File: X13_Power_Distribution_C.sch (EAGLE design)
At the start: 34 parts, among them Q1 IRF1018EPBF, Q2 310mA/60V/1.6Ω, Q3 IRF1018EPBF, Q4 IRF1018EPBF

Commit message: Version C! Uses connector C!
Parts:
- removed BRICK1, BRICK2: DIST2BRICK_B, Brick_Dist_Connector:DIST2BRICK_B
- added BRICK_A, BRICK_B: DIST2BRICK_C, Brick_Dist_Connector:DIST2BRICK_C
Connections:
- net +12V_A: now also BRICK_A.VOUT+; no longer BRICK1.VOUT+
- net +12V_B: now also BRICK_B.VOUT+; no longer BRICK2.VOUT+
- net +48V: now also BRICK_A.VIN+, BRICK_B.VIN+; no longer BRICK1.VIN+, BRICK2.VIN+
- net 12V_GND: now also BRICK_A.VOUT-, BRICK_B.VOUT-; no longer BRICK1.VOUT-, BRICK2.VOUT-
- net 48V_GND: now also BRICK_A.VIN-, BRICK_B.VIN-; no longer BRICK1.VIN-, BRICK2.VIN-
- net ALERT_1: now also BRICK_A.ALERT; no longer BRICK1.ALERT
- net ALERT_2: now also BRICK_B.ALERT; no longer BRICK2.ALERT
- net C2_1: now also BRICK_A.C2; no longer BRICK1.C2
- net C2_2: now also BRICK_B.C2; no longer BRICK2.C2
- net CLK: now also BRICK_A.CLK, BRICK_B.CLK; no longer BRICK1.CLK, BRICK2.CLK
- net DATA: now also BRICK_A.DATA, BRICK_B.DATA; no longer BRICK1.DATA, BRICK2.DATA
- net ON/OFF: now also BRICK_A.ON/OFF, BRICK_B.ON/OFF; no longer BRICK1.ON/OFF, BRICK2.ON/OFF
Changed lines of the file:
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@@
 <part name="H4" library="Mounting Holes" deviceset="6-32-HOLE" device="" package3d_urn="urn:adsk.eagle:package:24384748/2"/>
 <part name="CONVERSION" library="Dist_Convert_Connector" deviceset="DIST2CON" device=""/>
-<part name="BRICK2" library="Brick_Dist_Connector" deviceset="DIST2BRICK_B" device=""/>
-<part name="BRICK1" library="Brick_Dist_Connector" deviceset="DIST2BRICK_B" device=""/>
+<part name="BRICK_A" library="Brick_Dist_Connector" deviceset="DIST2BRICK_C" device=""/>
+<part name="BRICK_B" library="Brick_Dist_Connector" deviceset="DIST2BRICK_C" device=""/>
 </parts>
 <sheets>
@@
 <attribute name="NAME" x="40.64" y="27.432" size="1.27" layer="95"/>
 </instance>
-<instance part="BRICK2" gate="G$1" x="38.1" y="63.5" smashed="yes">
+<instance part="BRICK_A" gate="G$1" x="38.1" y="101.6" smashed="yes">
+<attribute name="NAME" x="38.608" y="110.236" size="1.778" layer="95"/>
+</instance>
+<instance part="BRICK_B" gate="G$1" x="38.1" y="63.5" smashed="yes">
 <attribute name="NAME" x="38.608" y="72.136" size="1.778" layer="95"/>
-</instance>
-<instance part="BRICK1" gate="G$1" x="38.1" y="101.6" smashed="yes">
-<attribute name="NAME" x="38.608" y="110.236" size="1.778" layer="95"/>
 </instance>
 </instances>
@@
 <wire x1="68.58" y1="106.68" x2="72.39" y2="106.68" width="0.1524" layer="91"/>
 <label x="72.39" y="106.68" size="1.778" layer="95" xref="yes"/>
-<pinref part="BRICK1" gate="G$1" pin="VOUT+"/>
+<pinref part="BRICK_A" gate="G$1" pin="VOUT+"/>
 </segment>
 </net>
@@
 <wire x1="68.58" y1="68.58" x2="72.39" y2="68.58" width="0.1524" layer="91"/>
 <label x="72.39" y="68.58" size="1.778" layer="95" xref="yes"/>
-<pinref part="BRICK2" gate="G$1" pin="VOUT+"/>
+<pinref part="BRICK_B" gate="G$1" pin="VOUT+"/>
 </segment>
 </net>
@@
 <wire x1="33.02" y1="91.44" x2="29.21" y2="91.44" width="0.1524" layer="91"/>
 <label x="29.21" y="91.44" size="1.778" layer="95" rot="R180" xref="yes"/>
-<pinref part="BRICK1" gate="G$1" pin="ON/OFF"/>
+<pinref part="BRICK_A" gate="G$1" pin="ON/OFF"/>
 </segment>
 <segment>
 <wire x1="33.02" y1="53.34" x2="29.21" y2="53.34" width="0.1524" layer="91"/>
 <label x="29.21" y="53.34" size="1.778" layer="95" rot="R180" xref="yes"/>
-<pinref part="BRICK2" gate="G$1" pin="ON/OFF"/>
+<pinref part="BRICK_B" gate="G$1" pin="ON/OFF"/>
 </segment>
 </net>
@@
 <wire x1="33.02" y1="106.68" x2="29.21" y2="106.68" width="0.1524" layer="91"/>
 <label x="29.21" y="106.68" size="1.778" layer="95" rot="R180" xref="yes"/>
-<pinref part="BRICK1" gate="G$1" pin="VIN+"/>
+<pinref part="BRICK_A" gate="G$1" pin="VIN+"/>
 </segment>
 <segment>
 <wire x1="33.02" y1="68.58" x2="29.21" y2="68.58" width="0.1524" layer="91"/>
 <label x="29.21" y="68.58" size="1.778" layer="95" rot="R180" xref="yes"/>
-<pinref part="BRICK2" gate="G$1" pin="VIN+"/>
+<pinref part="BRICK_B" gate="G$1" pin="VIN+"/>
 </segment>
 <segment>
@@
 <wire x1="33.02" y1="101.6" x2="29.21" y2="101.6" width="0.1524" layer="91"/>
 <label x="29.21" y="101.6" size="1.778" layer="95" rot="R180" xref="yes"/>
-<pinref part="BRICK1" gate="G$1" pin="VIN-"/>
+<pinref part="BRICK_A" gate="G$1" pin="VIN-"/>
 </segment>
 <segment>
 <wire x1="33.02" y1="63.5" x2="29.21" y2="63.5" width="0.1524" layer="91"/>
 <label x="29.21" y="63.5" size="1.778" layer="95" rot="R180" xref="yes"/>
-<pinref part="BRICK2" gate="G$1" pin="VIN-"/>
+<pinref part="BRICK_B" gate="G$1" pin="VIN-"/>
 </segment>
 <segment>
@@
 <wire x1="68.58" y1="86.36" x2="72.39" y2="86.36" width="0.1524" layer="91"/>
 <label x="72.39" y="86.36" size="1.778" layer="95" xref="yes"/>
-<pinref part="BRICK1" gate="G$1" pin="CLK"/>
+<pinref part="BRICK_A" gate="G$1" pin="CLK"/>
 </segment>
 <segment>
 <wire x1="68.58" y1="48.26" x2="72.39" y2="48.26" width="0.1524" layer="91"/>
 <label x="72.39" y="48.26" size="1.778" layer="95" xref="yes"/>
-<pinref part="BRICK2" gate="G$1" pin="CLK"/>
+<pinref part="BRICK_B" gate="G$1" pin="CLK"/>
 </segment>
 </net>
@@
 <wire x1="68.58" y1="96.52" x2="72.39" y2="96.52" width="0.1524" layer="91"/>
 <label x="72.39" y="96.52" size="1.778" layer="95" xref="yes"/>
-<pinref part="BRICK1" gate="G$1" pin="DATA"/>
+<pinref part="BRICK_A" gate="G$1" pin="DATA"/>
 </segment>
 <segment>
 <wire x1="68.58" y1="58.42" x2="72.39" y2="58.42" width="0.1524" layer="91"/>
 <label x="72.39" y="58.42" size="1.778" layer="95" xref="yes"/>
-<pinref part="BRICK2" gate="G$1" pin="DATA"/>
+<pinref part="BRICK_B" gate="G$1" pin="DATA"/>
 </segment>
 </net>
@@
 <wire x1="68.58" y1="101.6" x2="72.39" y2="101.6" width="0.1524" layer="91"/>
 <label x="72.39" y="101.6" size="1.778" layer="95" xref="yes"/>
-<pinref part="BRICK1" gate="G$1" pin="VOUT-"/>
+<pinref part="BRICK_A" gate="G$1" pin="VOUT-"/>
 </segment>
 <segment>
 <wire x1="68.58" y1="63.5" x2="72.39" y2="63.5" width="0.1524" layer="91"/>
 <label x="72.39" y="63.5" size="1.778" layer="95" xref="yes"/>
-<pinref part="BRICK2" gate="G$1" pin="VOUT-"/>
+<pinref part="BRICK_B" gate="G$1" pin="VOUT-"/>
 </segment>
 <segment>
@@
 <wire x1="68.58" y1="43.18" x2="72.39" y2="43.18" width="0.1524" layer="91"/>
 <label x="72.39" y="43.18" size="1.778" layer="95" xref="yes"/>
-<pinref part="BRICK2" gate="G$1" pin="C2"/>
+<pinref part="BRICK_B" gate="G$1" pin="C2"/>
 </segment>
 </net>
@@
 <wire x1="68.58" y1="81.28" x2="72.39" y2="81.28" width="0.1524" layer="91"/>
 <label x="72.39" y="81.28" size="1.778" layer="95" xref="yes"/>
-<pinref part="BRICK1" gate="G$1" pin="C2"/>
+<pinref part="BRICK_A" gate="G$1" pin="C2"/>
 </segment>
 </net>
@@
 <wire x1="68.58" y1="53.34" x2="72.39" y2="53.34" width="0.1524" layer="91"/>
 <label x="72.39" y="53.34" size="1.778" layer="95" xref="yes"/>
-<pinref part="BRICK2" gate="G$1" pin="ALERT"/>
+<pinref part="BRICK_B" gate="G$1" pin="ALERT"/>
 </segment>
 </net>
@@
 <wire x1="68.58" y1="91.44" x2="72.39" y2="91.44" width="0.1524" layer="91"/>
 <label x="72.39" y="91.44" size="1.778" layer="95" xref="yes"/>
-<pinref part="BRICK1" gate="G$1" pin="ALERT"/>
-</segment>
-</net>
+<pinref part="BRICK_A" gate="G$1" pin="ALERT"/>
+</segment>
+</net>

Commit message: Moved ON/OFF, moved a diode
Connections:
- net 48V_GND: now also D6.A
- net GND_RAW: no longer D6.A
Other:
- moved on the sheet: D6, Q1, R3
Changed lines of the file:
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@@
 <attribute name="VALUE" x="228.092" y="32.385" size="1.778" layer="96" font="vector" rot="R180" align="top-left"/>
 </instance>
-<instance part="Q1" gate="G$1" x="93.98" y="142.24" smashed="yes" rot="MR270">
-<attribute name="NAME" x="95.25" y="146.05" size="1.778" layer="95" font="vector" rot="MR0"/>
-<attribute name="VALUE" x="100.33" y="137.16" size="1.778" layer="96" font="vector" rot="MR0"/>
-</instance>
-<instance part="R3" gate="G$1" x="86.36" y="158.75" smashed="yes" rot="MR90">
-<attribute name="NAME" x="87.884" y="158.75" size="1.778" layer="95" font="vector" rot="MR90" align="bottom-center"/>
-<attribute name="VALUE" x="84.836" y="158.75" size="1.778" layer="96" font="vector" rot="MR90" align="top-center"/>
-</instance>
-<instance part="D6" gate="G$1" x="77.47" y="146.05" smashed="yes" rot="MR90">
-<attribute name="NAME" x="79.502" y="143.51" size="1.778" layer="95" font="vector" rot="MR90"/>
-<attribute name="VALUE" x="75.438" y="143.51" size="1.778" layer="96" font="vector" rot="MR90" align="top-left"/>
+<instance part="Q1" gate="G$1" x="81.28" y="142.24" smashed="yes" rot="MR270">
+<attribute name="NAME" x="82.55" y="146.05" size="1.778" layer="95" font="vector" rot="MR0"/>
+<attribute name="VALUE" x="87.63" y="137.16" size="1.778" layer="96" font="vector" rot="MR0"/>
+</instance>
+<instance part="R3" gate="G$1" x="87.63" y="158.75" smashed="yes" rot="MR90">
+<attribute name="NAME" x="89.154" y="158.75" size="1.778" layer="95" font="vector" rot="MR90" align="bottom-center"/>
+<attribute name="VALUE" x="86.106" y="158.75" size="1.778" layer="96" font="vector" rot="MR90" align="top-center"/>
+</instance>
+<instance part="D6" gate="G$1" x="95.25" y="146.05" smashed="yes" rot="MR90">
+<attribute name="NAME" x="97.282" y="143.51" size="1.778" layer="95" font="vector" rot="MR90"/>
+<attribute name="VALUE" x="93.218" y="143.51" size="1.778" layer="96" font="vector" rot="MR90" align="top-left"/>
 </instance>
 <instance part="D1" gate="G$1" x="148.59" y="161.29" smashed="yes" rot="R90">
@@
 <segment>
 <label x="68.58" y="166.37" size="1.778" layer="95" rot="R180" xref="yes"/>
-<wire x1="68.58" y1="166.37" x2="86.36" y2="166.37" width="0.1524" layer="91"/>
+<wire x1="68.58" y1="166.37" x2="87.63" y2="166.37" width="0.1524" layer="91"/>
 <pinref part="R3" gate="G$1" pin="2"/>
-<wire x1="86.36" y1="163.83" x2="86.36" y2="166.37" width="0.1524" layer="91"/>
+<wire x1="87.63" y1="163.83" x2="87.63" y2="166.37" width="0.1524" layer="91"/>
 </segment>
 <segment>
@@
 <segment>
 <pinref part="Q1" gate="G$1" pin="S"/>
-<wire x1="99.06" y1="139.7" x2="102.87" y2="139.7" width="0.1524" layer="91"/>
+<wire x1="86.36" y1="139.7" x2="95.25" y2="139.7" width="0.1524" layer="91"/>
 <label x="102.87" y="139.7" size="1.778" layer="95" rot="MR180" xref="yes"/>
+<pinref part="D6" gate="G$1" pin="A"/>
+<wire x1="95.25" y1="139.7" x2="102.87" y2="139.7" width="0.1524" layer="91"/>
+<wire x1="95.25" y1="143.51" x2="95.25" y2="139.7" width="0.1524" layer="91"/>
+<junction x="95.25" y="139.7"/>
 </segment>
 <segment>
@@
 </segment>
 <segment>
-<pinref part="D6" gate="G$1" pin="A"/>
-<wire x1="77.47" y1="143.51" x2="77.47" y2="139.7" width="0.1524" layer="91"/>
 <pinref part="Q1" gate="G$1" pin="D"/>
-<wire x1="88.9" y1="139.7" x2="77.47" y2="139.7" width="0.1524" layer="91"/>
-<wire x1="77.47" y1="139.7" x2="69.85" y2="139.7" width="0.1524" layer="91"/>
-<junction x="77.47" y="139.7"/>
+<wire x1="76.2" y1="139.7" x2="69.85" y2="139.7" width="0.1524" layer="91"/>
 <label x="69.85" y="139.7" size="1.778" layer="95" rot="R180" xref="yes"/>
 </segment>
@@
 <segment>
 <pinref part="R3" gate="G$1" pin="1"/>
-<wire x1="86.36" y1="153.67" x2="86.36" y2="151.13" width="0.1524" layer="91"/>
-<wire x1="86.36" y1="151.13" x2="77.47" y2="151.13" width="0.1524" layer="91"/>
+<wire x1="87.63" y1="153.67" x2="87.63" y2="151.13" width="0.1524" layer="91"/>
+<pinref part="Q1" gate="G$1" pin="G"/>
+<wire x1="83.82" y1="147.32" x2="83.82" y2="151.13" width="0.1524" layer="91"/>
+<wire x1="83.82" y1="151.13" x2="87.63" y2="151.13" width="0.1524" layer="91"/>
+<label x="95.25" y="152.4" size="0.8128" layer="95" rot="R180"/>
+<wire x1="87.63" y1="151.13" x2="95.25" y2="151.13" width="0.1524" layer="91"/>
+<junction x="87.63" y="151.13"/>
 <pinref part="D6" gate="G$1" pin="C"/>
-<wire x1="77.47" y1="148.59" x2="77.47" y2="151.13" width="0.1524" layer="91"/>
-<pinref part="Q1" gate="G$1" pin="G"/>
-<wire x1="96.52" y1="147.32" x2="96.52" y2="151.13" width="0.1524" layer="91"/>
-<wire x1="96.52" y1="151.13" x2="86.36" y2="151.13" width="0.1524" layer="91"/>
-<junction x="86.36" y="151.13"/>
-<label x="96.52" y="152.4" size="0.8128" layer="95" rot="R180"/>
-</segment>
-</net>
+<wire x1="95.25" y1="151.13" x2="95.25" y2="148.59" width="0.1524" layer="91"/>
+</segment>
+</net>

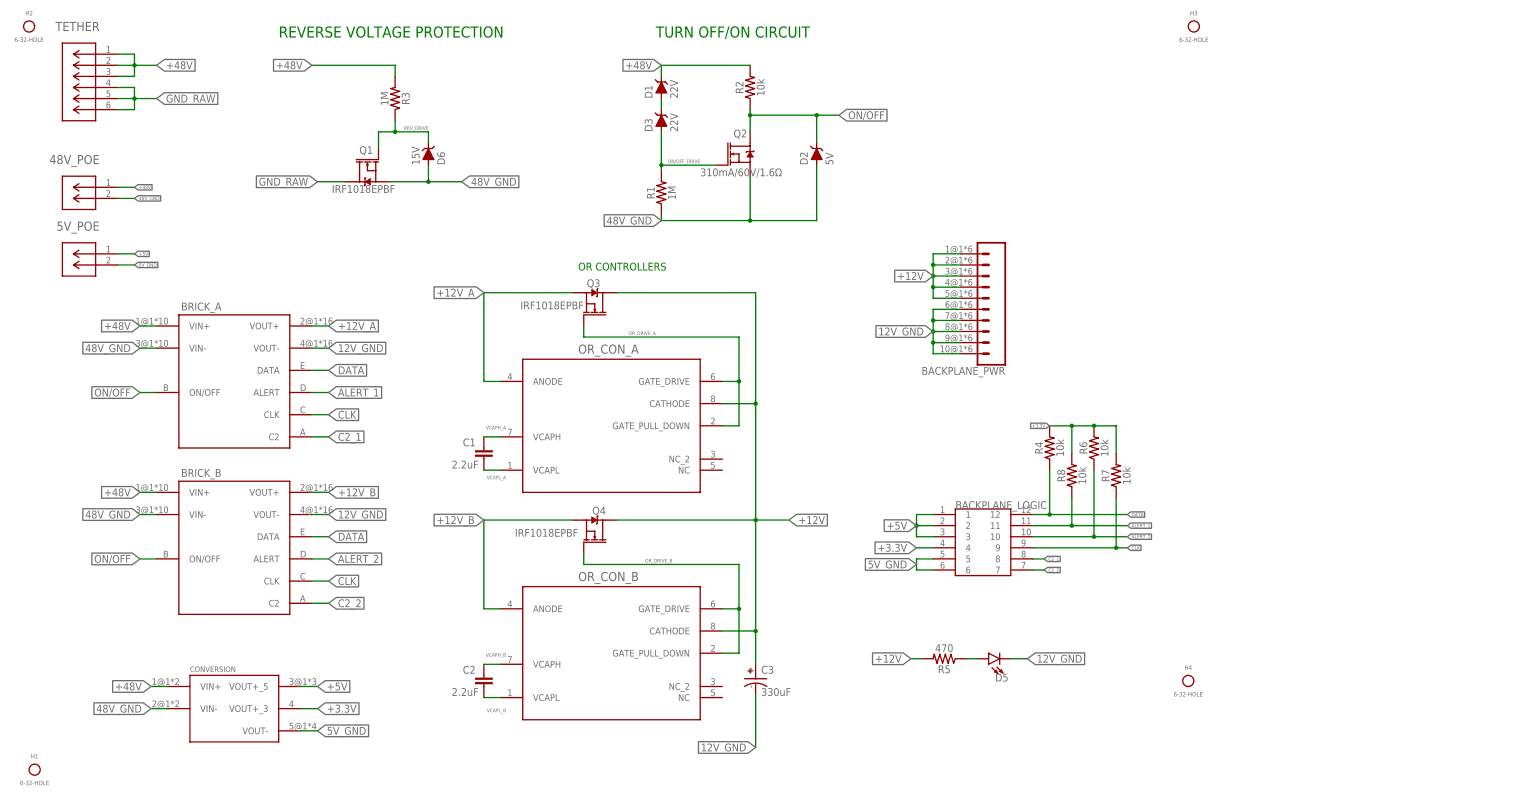
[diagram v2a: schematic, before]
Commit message: Two LEDs where once was one
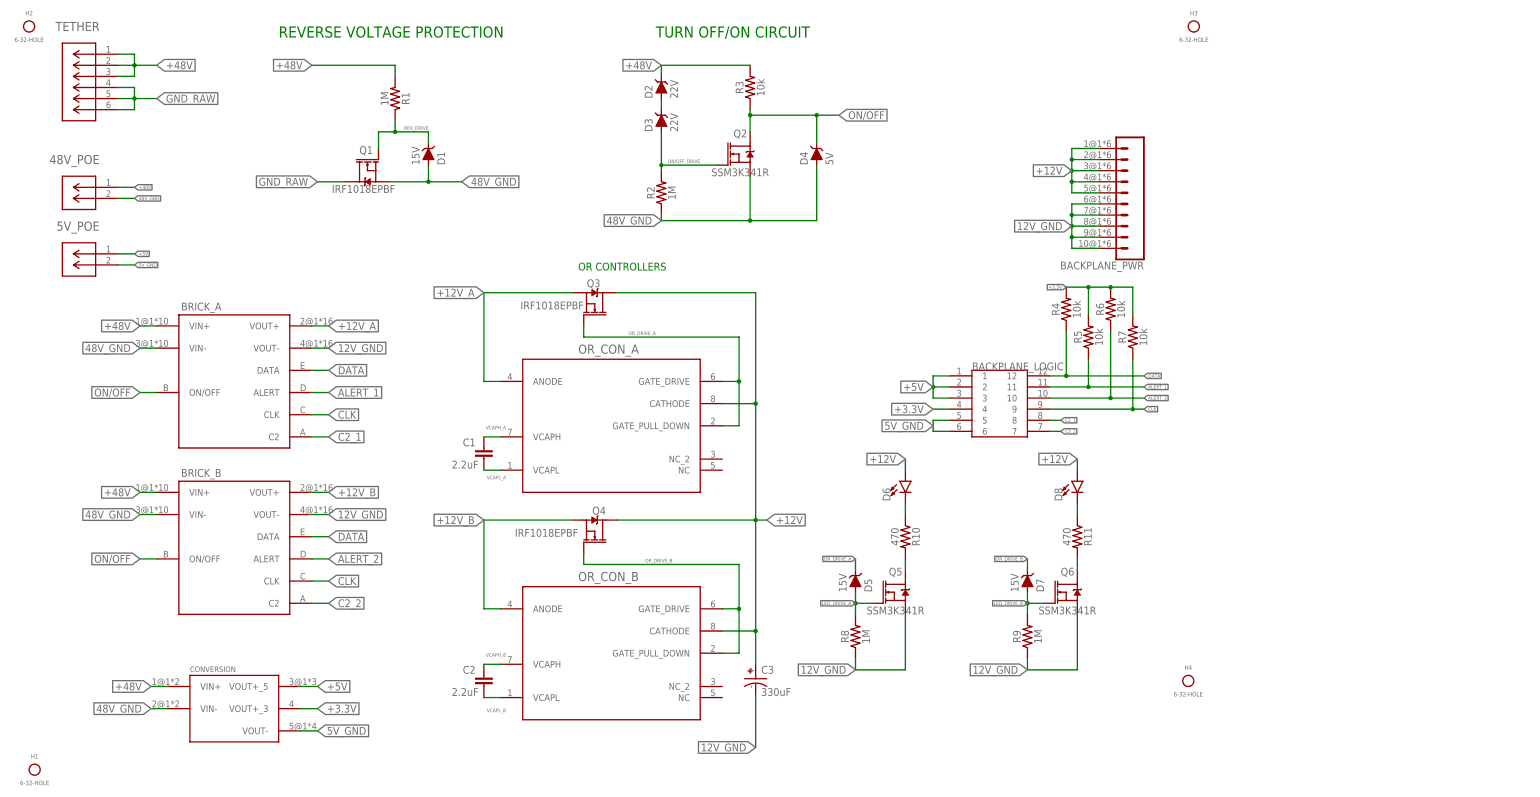
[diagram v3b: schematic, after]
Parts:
- added D4: 5V, SparkFun-DiscreteSemi:DIODE-ZENER-BZT52C3V6S
- added D7: 15V, SparkFun-DiscreteSemi:DIODE-ZENER-BZT52C3V6S
- added D8: (no value), SparkFun-LED:LED0603
- added Q5, Q6: SSM3K341R, SparkFun-DiscreteSemi:MOSFET-NCH-2N7002PW
- added R10, R11: 470, SparkFun-Resistors:RESISTOR0603
- added R9: 1M, SparkFun-Resistors:RESISTOR0603
- D1: value 22V -> 15V
- D2: value 5V -> 22V
- D5: value (none) -> 15V; device SparkFun-LED:LED0603 -> SparkFun-DiscreteSemi:DIODE-ZENER-BZT52C3V6S
- D6: value 15V -> (none); device SparkFun-DiscreteSemi:DIODE-ZENER-BZT52C3V6S -> SparkFun-LED:LED0603
- Q2: value 310mA/60V/1.6Ω -> SSM3K341R
- R1: SPICEPREFIX R -> (none)
- R2: value 10k -> 1M
- R3: value 1M -> 10k; SPICEPREFIX (none) -> R
- R5: value 470 -> 10k
- R8: value 10k -> 1M; SPICEPREFIX (none) -> R
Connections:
- removed net N$8: D5.A, R5.1
- new net LED_DRIVE_A: D5.A, Q5.G, R8.2
- new net LED_DRIVE_B: D7.A, Q6.G, R9.2
- new net N$4: Q5.D, R10.2
- new net N$5: D6.C, R10.1
- new net N$6: Q6.D, R11.2
- new net N$7: D8.C, R11.1
- net +12V: now also D6.A, D8.A; no longer R5.2
- net +3.3V: now also R5.2; no longer R8.2
- net +48V: now also D2.C, R1.2; no longer D1.C, R2.2
- net 12V_GND: now also Q5.S, Q6.S, R8.1, R9.1; no longer D5.C
- net 48V_GND: now also D1.A, D4.A, R2.1; no longer D2.A, D6.A, R1.1
- net ALERT_1: now also R5.1; no longer R8.1
- net N$1: now also D2.A; no longer D1.A
- net ON/OFF: now also D4.C, R3.1; no longer D2.C, R2.1
- net ON/OFF_DRIVE: now also R2.2; no longer R1.2
- net OR_DRIVE_A: now also D5.C
- net OR_DRIVE_B: now also D7.C
- net REV_DRIVE: now also D1.C, R1.1; no longer D6.C, R3.1
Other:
- moved on the sheet: BACKPLANE_LOGIC, BACKPLANE_PWR, D1, D2, R1, R2, R3, R4, R5, R6, R7, R8

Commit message: Some tweaks and labeling
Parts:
- R10: value 470 -> 1M; SPICEPREFIX (none) -> R
- R9: value 1M -> 470; SPICEPREFIX R -> (none)
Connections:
- net 12V_GND: now also R10.1; no longer R9.1
- net LED_DRIVE_B: now also R10.2; no longer R9.2
- net N$4: now also R9.2; no longer R10.2
- net N$5: now also R9.1; no longer R10.1
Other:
- note added: "BACKPLANE CONNECTORS"
- note added: "BRICK CONNECTORS"
- note added: "OR MOSFET CONTROLLERS"
- note added: "OR MOSFET INDICATOR LEDS"
- note removed: "OR CONTROLLERS"
- moved on the sheet: BACKPLANE_LOGIC, BACKPLANE_PWR, D5, D6, D7, D8, Q5, Q6, R10, R11, R4, R5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

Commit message: Added LM5050, tweaks
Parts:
- added IC3, IC4: LM5050, Dist_OR_Controller:DIST_OR_CONTROL_ALTMK06A-M
- BACKPLANE_LOGIC: value IPL1-107-01-L-D-RE-P -> IPL1-106-01-L-D-RE1-K; device Backplane_Dist_Logic_Connector:IPL1-107-01-L-D-RE-P -> Backplane_Dist_Logic_Connector:IPL1-106-01-L-D-RE1-K
- IC1, IC2: value DIST_OR_DIODEDGK0008A_M -> LM74610
- renumbered OR_CON_A to IC1, OR_CON_B to IC2
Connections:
- net +12V: now also IC3.OUT, IC3.VS, IC4.OUT, IC4.VS
- net +12V_A: now also IC3.IN
- net +12V_B: now also IC4.IN
- net 12V_GND: now also IC3.GND, IC4.GND
- net OR_DRIVE_A: now also IC3.GATE
- net OR_DRIVE_B: now also IC4.GATE
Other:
- note added: "OR CONTROLLER ALTERNATIVE"
